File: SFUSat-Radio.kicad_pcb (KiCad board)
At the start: 2 copper layers, 95.9 x 90.2 mm, 81 parts, among them J1 PC104-8BIT, J2 PC104PTH, J3 PC104PTH, J4 PC104PTH, J5 PC104PTH, J6 SMA, J7 SMA, J8 SMA, J9 SMA, P1 CONN_02X05, P2 CONN_01X03, P3 CONN_01X03, P4 CONN_01X03, U1 2N7002DW, U10 RT9183, U2 CC1101-Q1, U3 0433BM15A0001, U4 SINGLE_0402, U5 SKY13372-467LF, U6 SINGLE_0402, U7 SINGLE_0402, U8 SKY65366-21, U9 TPS799, X1 NX3225GA

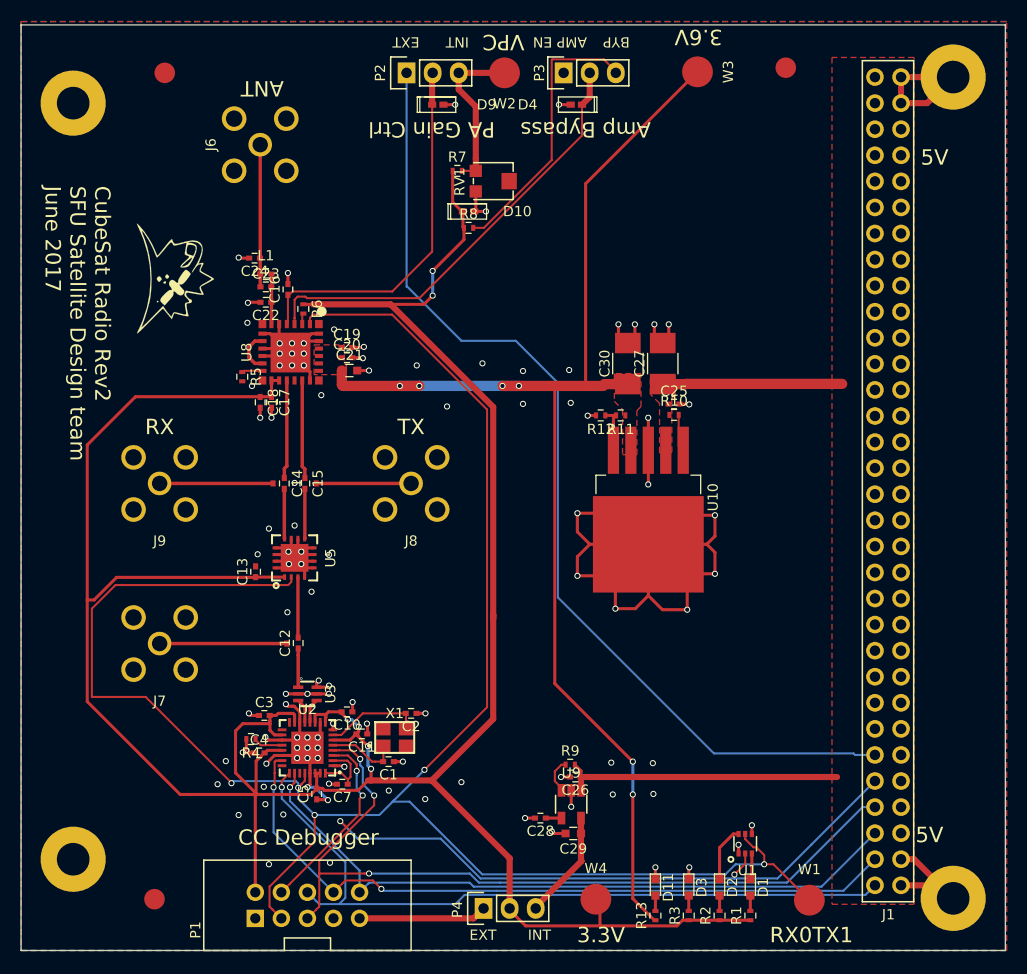
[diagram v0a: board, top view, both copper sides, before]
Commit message: fixed labels, via stitching
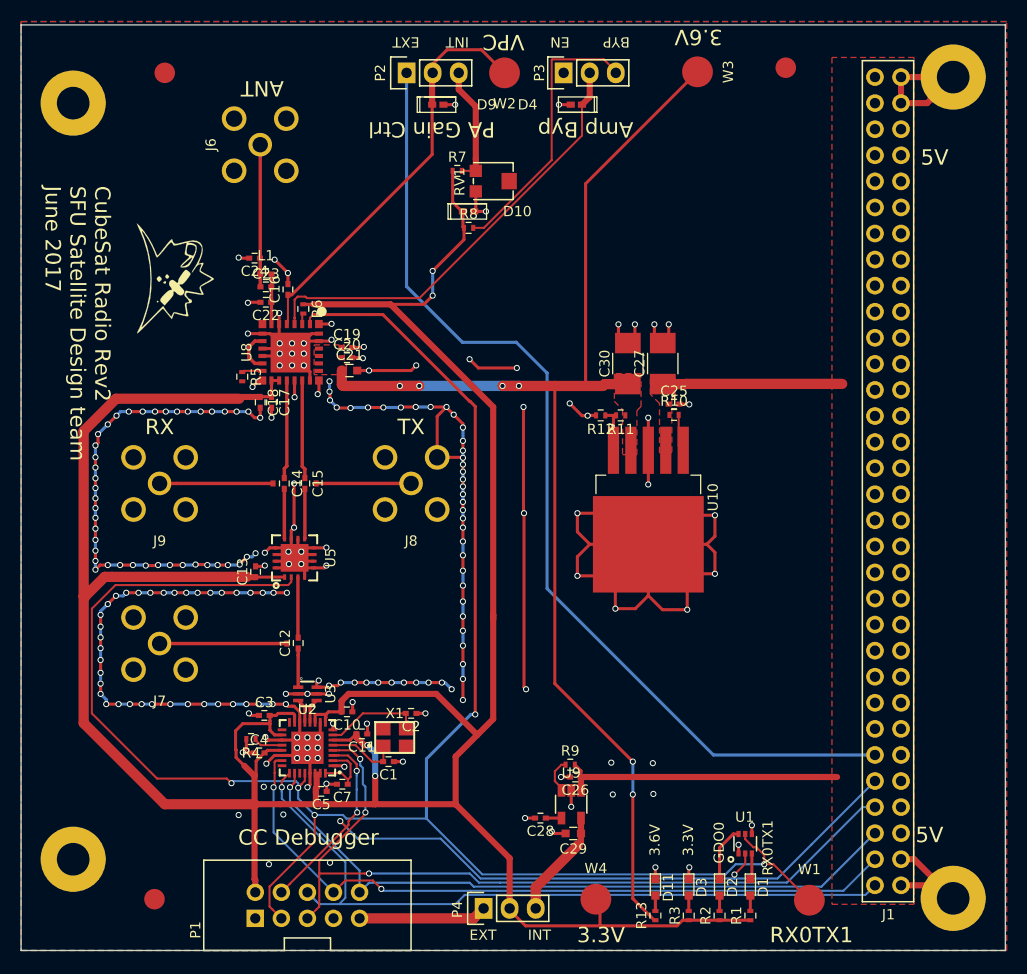
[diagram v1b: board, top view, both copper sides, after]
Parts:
- moved C5 0.51 mm to (141.8, 133.0), turned to 180 degrees
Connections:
- W2 pad 1: Net-(P2-Pad3) -> /Front_End/VPC
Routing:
- net GND: track 219.7 -> 433.4 mm, vias 74 -> 218
- net /VDD_3.3: track 277.1 -> 295.9 mm, vias 6 -> 4
- net Net-(P2-Pad3): track 16.0 -> 11.6 mm
- net /Front_End/VPC: track 36.1 -> 40.0 mm
- net /GPIO2: track 192.8 -> 191.4 mm
- net /~CS: track 79.4 -> 78.6 mm
- net (no net): vias 33 -> 9
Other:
- board text added: "Amp Byp"
- board text added: "EN"
- board text added: "GDO0"
- board text removed: "AMP EN"
- board text removed: "Amp Bypass"

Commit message: more via stitching
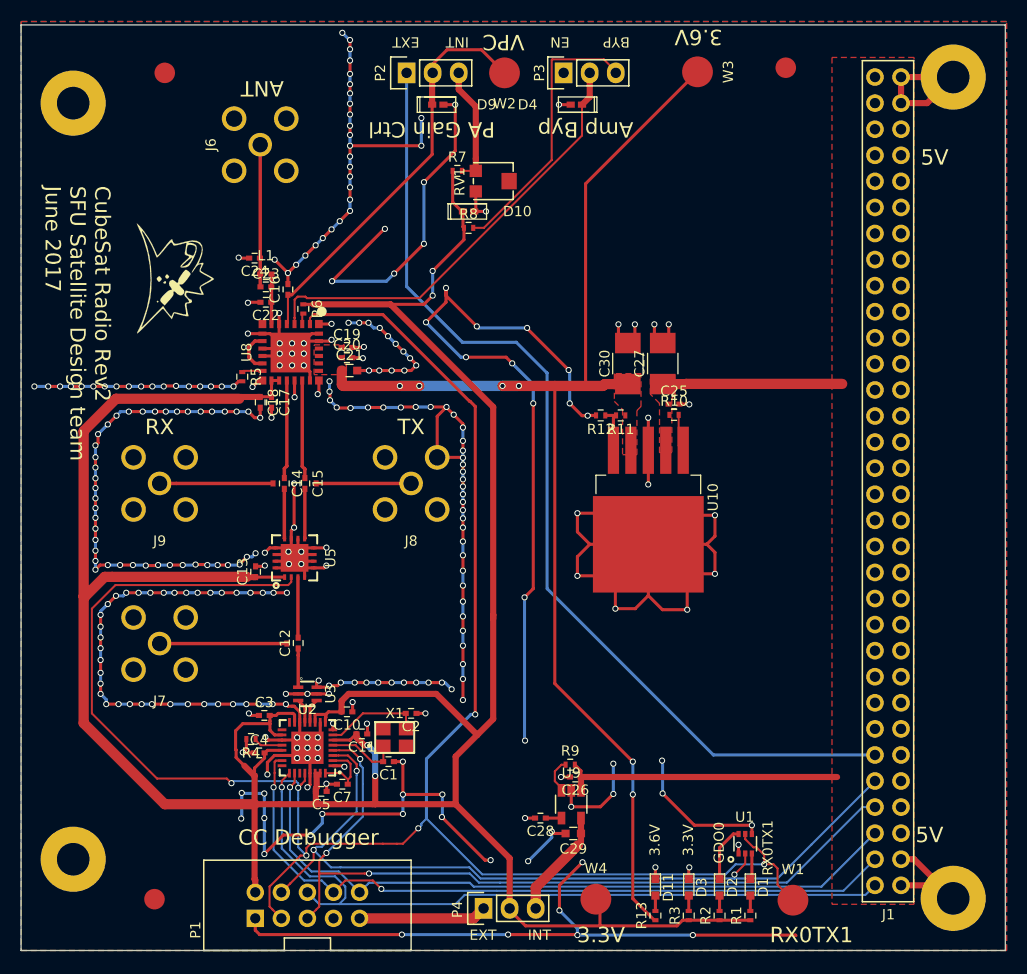
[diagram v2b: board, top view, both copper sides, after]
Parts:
- moved W1 1.60 mm to (187.7, 143.6)
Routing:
- net GND: track 433.4 -> 701.8 mm, vias 218 -> 306
- net /GPIO2: track 191.4 -> 193.0 mm, vias 5 -> 6
- net /MISO: track 67.5 -> 69.1 mm
- net /SCLK: track 72.4 -> 73.8 mm
- net /MOSI: track 70.9 -> 71.9 mm
- net /GPIO0: track 80.3 -> 81.2 mm, vias 4 -> 3
- net (no net): vias 9 -> 0

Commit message: placed component ref
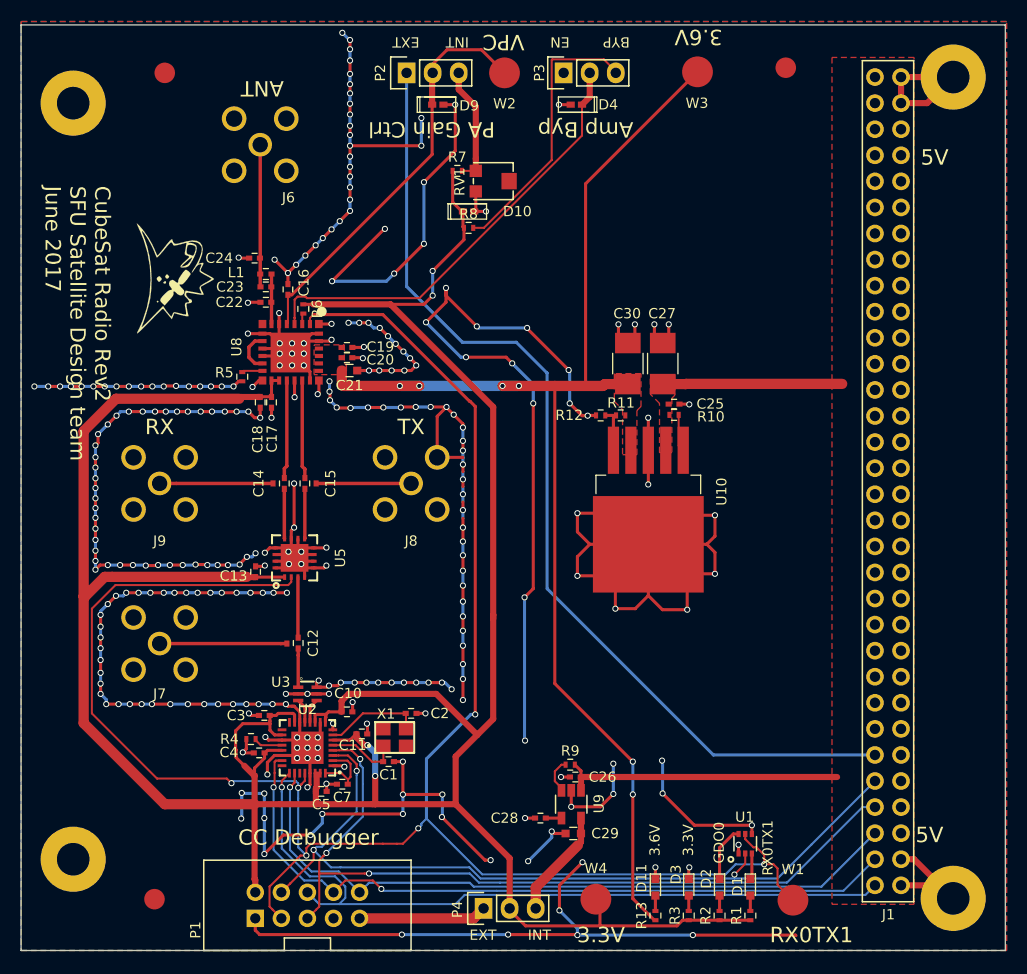
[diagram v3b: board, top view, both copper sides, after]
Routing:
- net GND: vias 306 -> 301

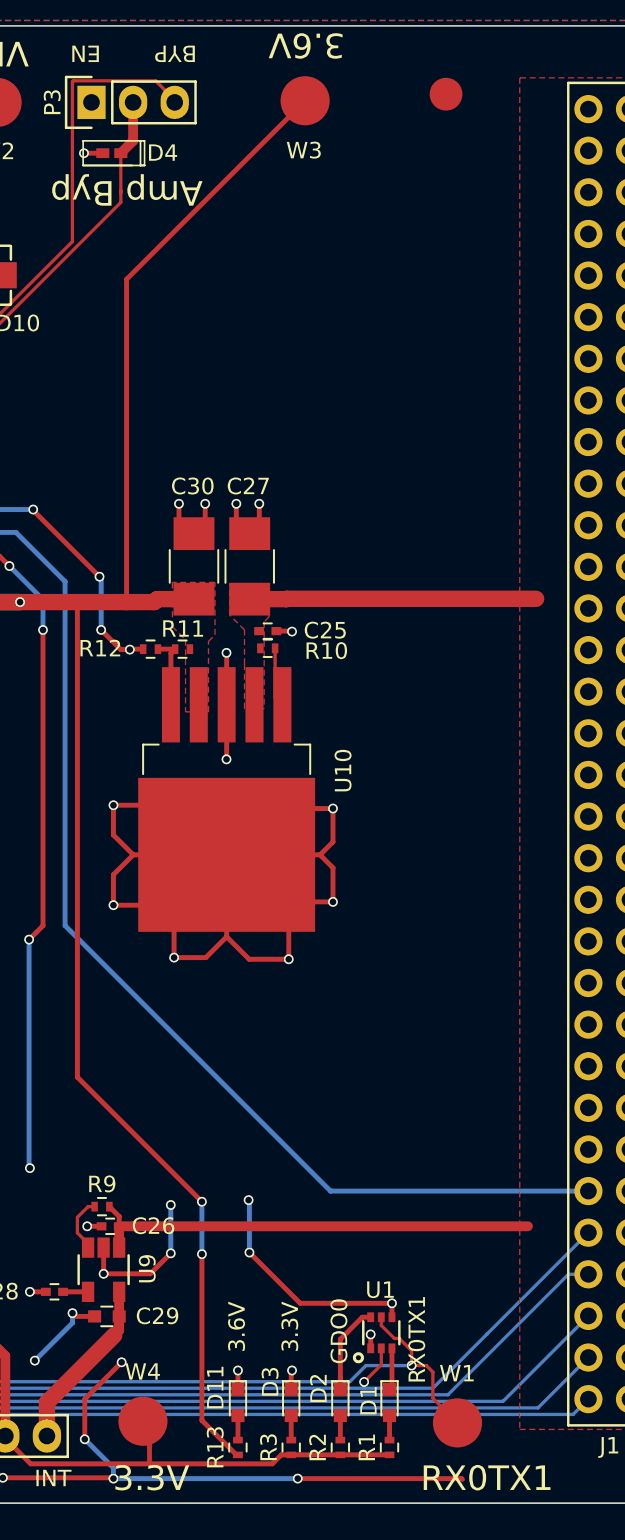
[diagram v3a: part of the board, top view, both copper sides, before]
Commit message: added TVS to TP
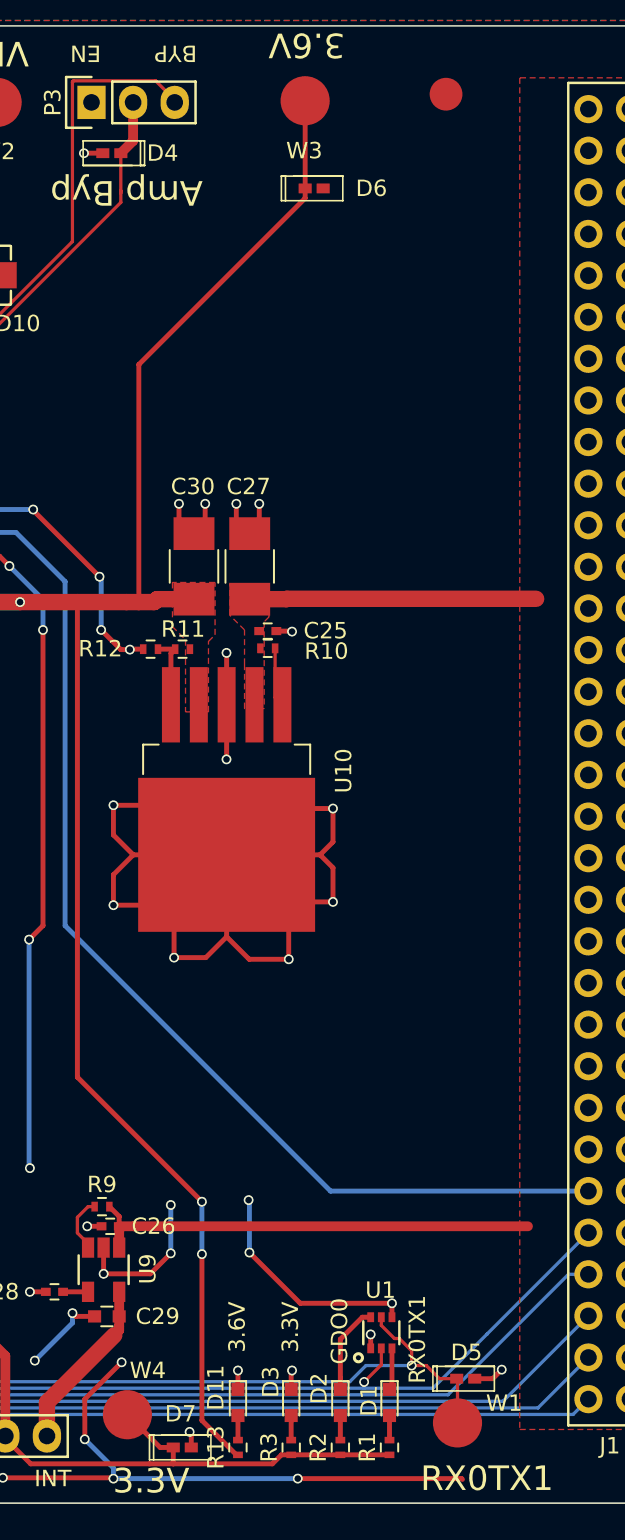
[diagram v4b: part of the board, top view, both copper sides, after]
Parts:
- added D5: PESD5Zx, SFUSat:PESD57zx, F.Cu at (188.2, 140.9)
- added D6: PESD5Zx, SFUSat:PESD57zx, F.Cu at (178.9, 68.2)
- added D7: PESD5Zx, SFUSat:PESD57zx, F.Cu at (170.9, 145.1)
- moved W4 1.03 mm to (167.6, 143.1)
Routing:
- net (no net): track 0.00 -> 22.2 mm, vias 0 -> 15
- net GND: track 701.8 -> 682.4 mm, vias 301 -> 288
- net /VDD_3.3: track 296.1 -> 299.1 mm
- net /GPIO2: track 193.0 -> 193.6 mm
